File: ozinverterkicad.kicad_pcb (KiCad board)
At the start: 2 copper layers, 100 x 100 mm, 83 parts, among them P1 CONN_02X05, P2 status, P3 on/off, P4 temp, P5 ct sense, P6 Active mains, P7 neutral mains, P8 systemled, Q2 tip35c, T1 12vac transforme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

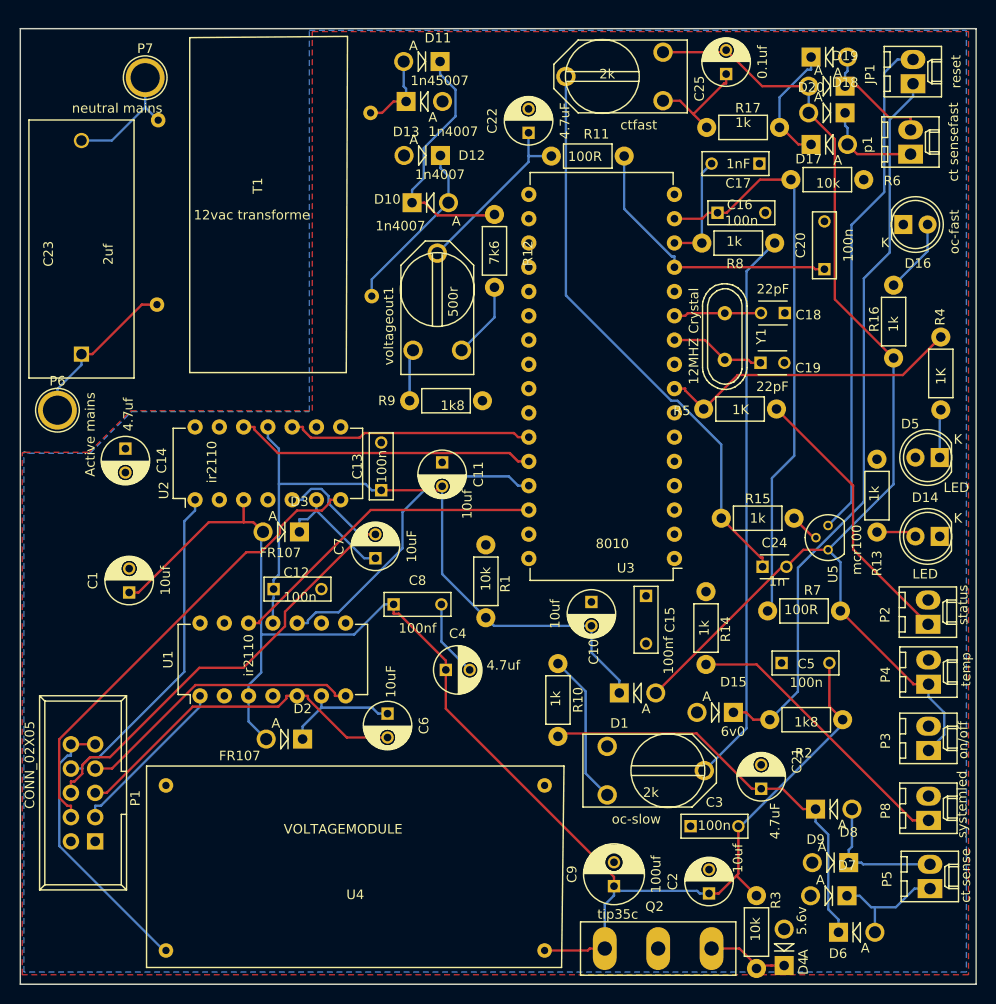
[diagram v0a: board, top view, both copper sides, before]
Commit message: changedboard outline to under 100x100
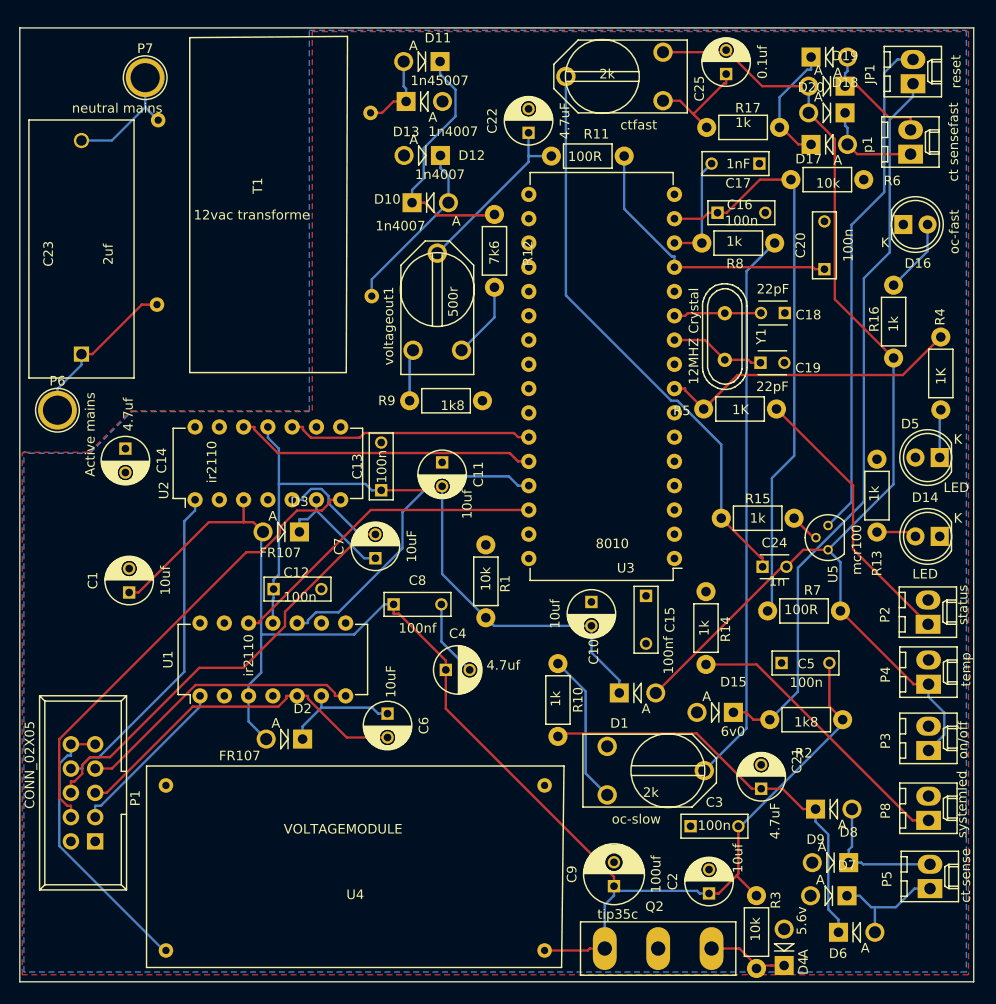
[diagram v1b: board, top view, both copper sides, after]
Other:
- board size 100 x 100 mm -> 99.8 x 99.8 mm
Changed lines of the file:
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@@
     (links 170)
     (no_connects 2)
-    (area 74.143799 50.801199 174.319001 150.951001)
+    (area 74.092999 50.724999 174.319001 150.697001)
     (thickness 1.6)
     (drawings 4)
@@
     (pcbplotparams
       (layerselection 0x010f0_80000001)
-      (usegerberextensions false)
+      (usegerberextensions true)
       (excludeedgelayer true)
       (linewidth 0.100000)
@@
       (padsonsilk false)
       (subtractmaskfromsilk false)
-      (outputformat 4)
+      (outputformat 1)
       (mirror false)
       (drillshape 0)
@@
     )
   )
-  (gr_line (start 74.2188 150.876) (end 74.2188 50.8762) (angle 90) (layer Edge.Cuts) (width 0.15))
-  (gr_line (start 174.244 150.876) (end 74.2188 150.876) (angle 90) (layer Edge.Cuts) (width 0.15))
-  (gr_line (start 174.244 50.8762) (end 174.244 150.876) (angle 90) (layer Edge.Cuts) (width 0.15))
-  (gr_line (start 74.2188 50.8762) (end 174.244 50.8762) (angle 90) (layer Edge.Cuts) (width 0.15))
+  (gr_line (start 74.168 50.8) (end 173.99 50.8) (angle 90) (layer Edge.Cuts) (width 0.15))
+  (gr_line (start 74.168 150.622) (end 74.168 50.8) (angle 90) (layer Edge.Cuts) (width 0.15))
+  (gr_line (start 173.99 150.622) (end 74.168 150.622) (angle 90) (layer Edge.Cuts) (width 0.15))
+  (gr_line (start 173.99 50.8) (end 173.99 150.622) (angle 90) (layer Edge.Cuts) (width 0.15))
   (segment (start 133.604 147.345) (end 133.807 147.142) (width 0.25) (layer F.Cu) (net 1))
   (segment (start 129.083 147.345) (end 133.604 147.345) (width 0.25) (layer F.Cu) (net 1))

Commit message: changed plug around for correct pinout
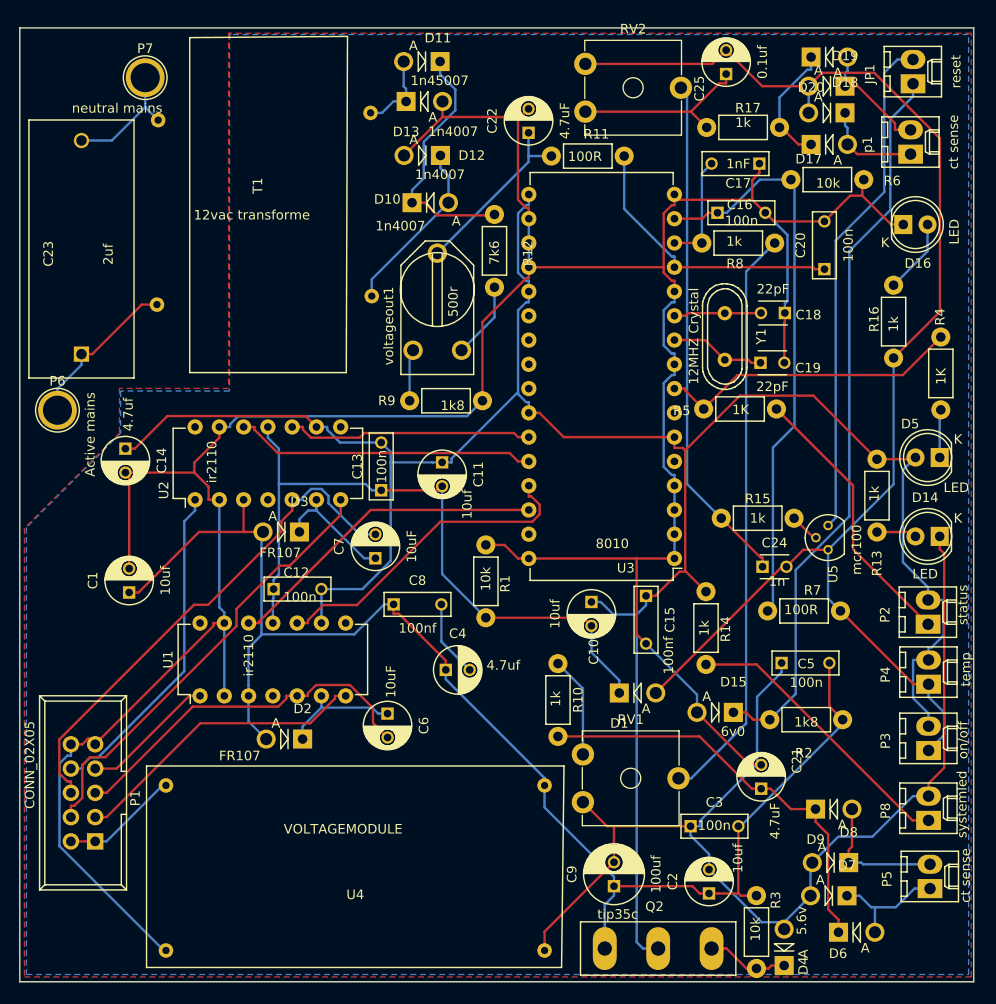
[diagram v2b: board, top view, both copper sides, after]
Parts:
- removed ctfast, oc-slow: 2k, Discret:RV2X4
- added RV1: 2k, Potentiometers:Potentiometer_Trimmer_ACP_CA9v_Horizontal_Px10.0mm_Py5.0mm, F.Cu at (133.1, 131.8)
- added RV2: 2k, Potentiometers:Potentiometer_Trimmer_ACP_CA9v_Horizontal_Px10.0mm_Py5.0mm, F.Cu at (133.3, 59.6)
- D16: value oc-fast -> LED
- p1: value ct sensefast -> ct sense
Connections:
- P1 pad 1: GND -> +48V
- P1 pad 10: +48V -> GND
- P1 pad 2: GND -> +48V
- P1 pad 9: +48V -> GND
- U1 pad 1: Net-(P1-Pad3) -> Net-(P1-Pad7)
- U1 pad 7: Net-(P1-Pad7) -> Net-(P1-Pad3)
- U4 pad 1: +12V -> GND
- U4 pad 2: GND -> +12V
- U4 pad 3: GND -> +48V
- U4 pad 4: +48V -> GND
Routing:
- net GND: track 0.00 -> 446.6 mm
- net +5V: track 0.00 -> 244.1 mm
- net Net-(C24-Pad2): track 123.8 -> 145.3 mm
- net +48V: track 29.6 -> 12.4 mm
- net Net-(P1-Pad7): track 30.5 -> 14.1 mm
- net Net-(P1-Pad3): track 17.6 -> 31.6 mm
- net Net-(C25-Pad1): track 11.5 -> 19.3 mm
- net Net-(C24-Pad1): track 60.3 -> 53.8 mm
- net +12V: track 155.0 -> 149.1 mm
- net Net-(R10-Pad2): track 15.9 -> 10.6 mm
- net Net-(C7-Pad2): track 56.9 -> 54.1 mm
- net Net-(R8-Pad1): track 58.3 -> 61.0 mm
- net Net-(P1-Pad4): track 49.2 -> 46.7 mm
- net Net-(C6-Pad2): track 36.9 -> 38.8 mm
- net Net-(U1-Pad10): track 33.4 -> 33.9 mm
